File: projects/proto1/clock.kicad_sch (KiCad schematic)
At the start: 7 parts, among them U24 MX8315MC, X1 10M, X2 8M, X3 3.6864M, X4 8M, Y1 14.31818M

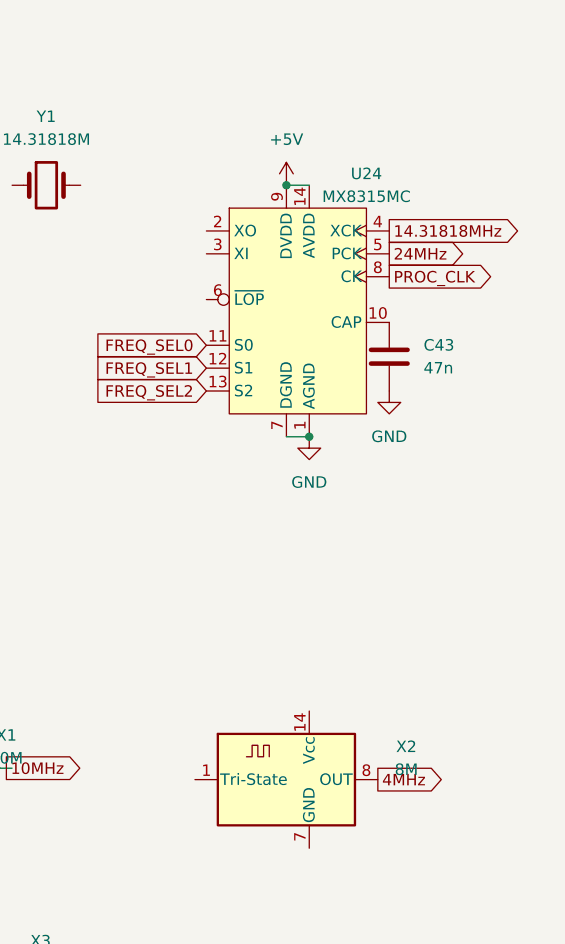
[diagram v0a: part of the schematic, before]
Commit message: Renamed CMC to SCU, changed verification method to cocotb, and modified pcb schematic
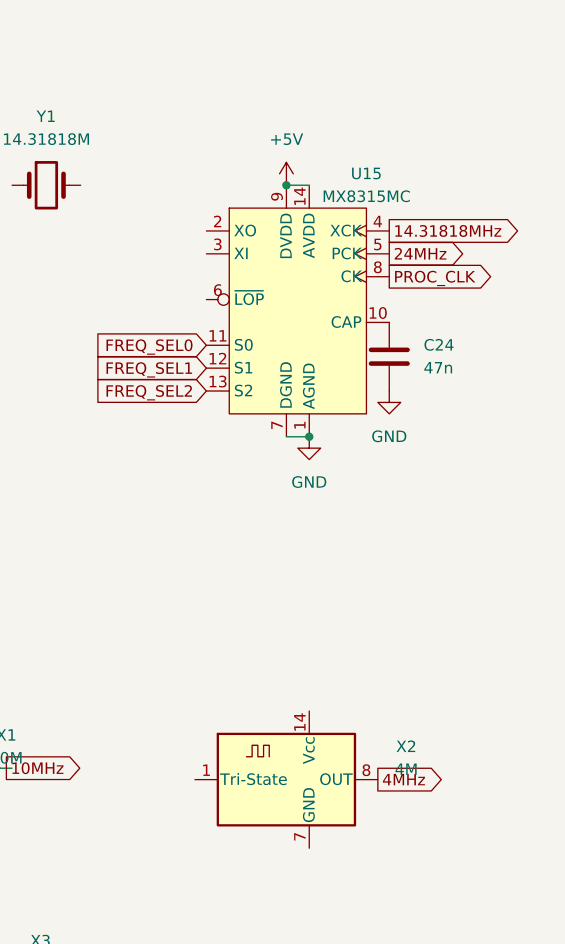
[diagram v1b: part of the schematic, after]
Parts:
- X2: value 8M -> 4M
- renumbered C43 to C24, U24 to U15
